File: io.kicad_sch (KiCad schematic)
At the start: 35 parts, among them K2 TIANBO-HJR-4102-L, K3 TIANBO-HJR-4102-L, K4 TIANBO-HJR-4102-L, K5 TIANBO-HJR-4102-L, K6 TIANBO-HJR-4102-L, K7 TIANBO-HJR-4102-L, K8 AQY210S, Q2 BSS138, Q3 BSS138, Q4 BSS138, Q5 BSS138, Q6 BSS138, Q7 BSS138, U10 74HC595, X5 Conn_Rel2, X6 Conn_Rel1

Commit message: Redesign PCB
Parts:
- removed D11: LED1, LED_SMD:LED_PLCC-2, symbol Device:LED_Small
- removed K8: AQY210S, SamacSys_Parts:SOP254P962X275-4N, symbol SamacSys_Parts:AQY210S
- removed R19, R24: 180R, Resistor_SMD:R_0603_1608Metric, symbol Device:R_Small
- added C60: 100n, Capacitor_SMD:C_0603_1608Metric, symbol Device:C_Small
- added J10: JP_REL1_COM_12V, Connector_PinHeader_2.54mm:PinHeader_1x02_P2.54mm_Vertical, symbol Connector:Conn_01x02_Male
- added J12: JP_REL2_COM_12V, Connector_PinHeader_2.54mm:PinHeader_1x02_P2.54mm_Vertical, symbol Connector:Conn_01x02_Male
- added J13: JP_REL3_COM_12V, Connector_PinHeader_2.54mm:PinHeader_1x02_P2.54mm_Vertical, symbol Connector:Conn_01x02_Male
- added J14: Conn_REL1, Connector_PinHeader_2.54mm:PinHeader_1x03_P2.54mm_Vertical, symbol Connector:Conn_01x03_Male
- added J15: Conn_REL2, Connector_PinHeader_2.54mm:PinHeader_1x03_P2.54mm_Vertical, symbol Connector:Conn_01x03_Male
- added J16: Conn_REL3, Connector_PinHeader_2.54mm:PinHeader_1x03_P2.54mm_Vertical, symbol Connector:Conn_01x03_Male
- added J5: JP_REL4_COM_12V, Connector_PinHeader_2.54mm:PinHeader_1x02_P2.54mm_Vertical, symbol Connector:Conn_01x02_Male
- added J8: JP_REL5_COM_12V, Connector_PinHeader_2.54mm:PinHeader_1x02_P2.54mm_Vertical, symbol Connector:Conn_01x02_Male
- added J9: JP_REL6_COM_12V, Connector_PinHeader_2.54mm:PinHeader_1x02_P2.54mm_Vertical, symbol Connector:Conn_01x02_Male
- added JP29: JP_REL_VCC, Jumper:SolderJumper-3_P1.3mm_Open_RoundedPad1.0x1.5mm, symbol Jumper:SolderJumper_3_Open
- added R74, R75, R76, R77, R78, R79: 4k7, Resistor_SMD:R_0603_1608Metric, symbol Device:R_Small
- added U20: HC 151, Package_SO:SOIC-16_3.9x9.9mm_P1.27mm, symbol 74xx_IEEE:74151
- Q5, Q6, Q7: value BSS138 -> IRLML 2502
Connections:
- net DO1_1 is gone; now on net REL6_COM: X5.7 (Pin_7)
- net DO1_2 is gone; now on net REL6_NO: X5.8 (Pin_8)
- net +3V3: now also C60.1, R74.2, R75.2, R76.2, R77.2, R78.2, R79.2, U20.16 (VCC)
- net +5V: now also JP29.1 (A); no longer D10.1 (K), D5.1 (K), D6.1 (K), D7.1 (K), D8.1 (K), D9.1 (K), K2.5, K3.5, K4.5, K5.5, K6.5, K7.5
- net GND: now also C60.2, U20.7 (~{E}), U20.8 (GND); no longer X5.9 (Pin_9)
- net REL1_COM: now also J10.1 (Pin_1)
- net REL1_NC: now also J14.3 (Pin_3); no longer X6.2 (Pin_2)
- net REL1_NO: now also X6.2 (Pin_2); no longer X6.3 (Pin_3)
- net REL2_COM: now also J12.1 (Pin_1)
- net REL2_NC: now also J15.3 (Pin_3); no longer X6.5 (Pin_5)
- net REL2_NO: now also X6.5 (Pin_5); no longer X6.6 (Pin_6)
- net REL3_COM: now also J13.1 (Pin_1)
- net REL3_NC: now also J16.3 (Pin_3); no longer X6.8 (Pin_8)
- net REL3_NO: now also X6.8 (Pin_8); no longer X6.9 (Pin_9)
- net REL4_COM: now also J5.1 (Pin_1)
- net REL5_COM: now also X5.4 (Pin_4), J8.1 (Pin_1); no longer X5.3 (Pin_3)
- net REL5_NO: now also X5.5 (Pin_5); no longer X5.4 (Pin_4)
- net REL6_COM: now also J9.1 (Pin_1); no longer X5.5 (Pin_5)
- net REL6_NO: no longer X5.6 (Pin_6)
- net T_ADDR1: now reaches U10.7 (QH)
- net T_ADDR1: now also U20.10 (S1)
- net DO1 renamed T_ADDR0
- net T_ADDR0: now also U20.11 (S0)
- new net REL1_NC_TACHO: J14.2 (Pin_2), X6.3 (Pin_3)
- new net REL2_NC_TACHO: J15.2 (Pin_2), X6.6 (Pin_6)
- new net REL3_NC_TACHO: J16.2 (Pin_2), X6.9 (Pin_9)
- new net TACHO: U20.5 (Q)
- new net TACHO1: J14.1 (Pin_1), R74.1, U20.4 (I0)
- new net TACHO2: J15.1 (Pin_1), R75.1, U20.3 (I1)
- new net TACHO3: J16.1 (Pin_1), R76.1, U20.2 (I2)
- new net TACHO4: R77.1, U20.1 (I3), X5.3 (Pin_3)
- new net TACHO5: R78.1, U20.15 (I4), X5.6 (Pin_6)
- new net TACHO6: R79.1, U20.14 (I5), X5.9 (Pin_9)
- new net T_ADDR2: U20.9 (S2)
- new net VCC_REL: D10.1 (K), D5.1 (K), D6.1 (K), D7.1 (K), D8.1 (K), D9.1 (K), JP29.2 (C), K2.5, K3.5, K4.5, K5.5, K6.5, K7.5
- new net V_IN: J10.2 (Pin_2), J12.2 (Pin_2), J13.2 (Pin_2), J5.2 (Pin_2), J8.2 (Pin_2), J9.2 (Pin_2), JP29.3 (B)
- no-connect marks 0 -> 3
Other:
- note added: "12V Eingangsspannung auf COM des Relais"
- note added: "J15 - J16: NC des Relais oder Tachosignal auf Stecker"
- note added: "Je nach Relaistyp kann eine Spulenspannung von 5V oder 12V gewählt werden. Wichtig hierfür ist, dass die Bestückung der DC/DC auf Seite beachtet wrid."
- moved on the sheet: C17, C18, R22, R23, U10, X5, X6

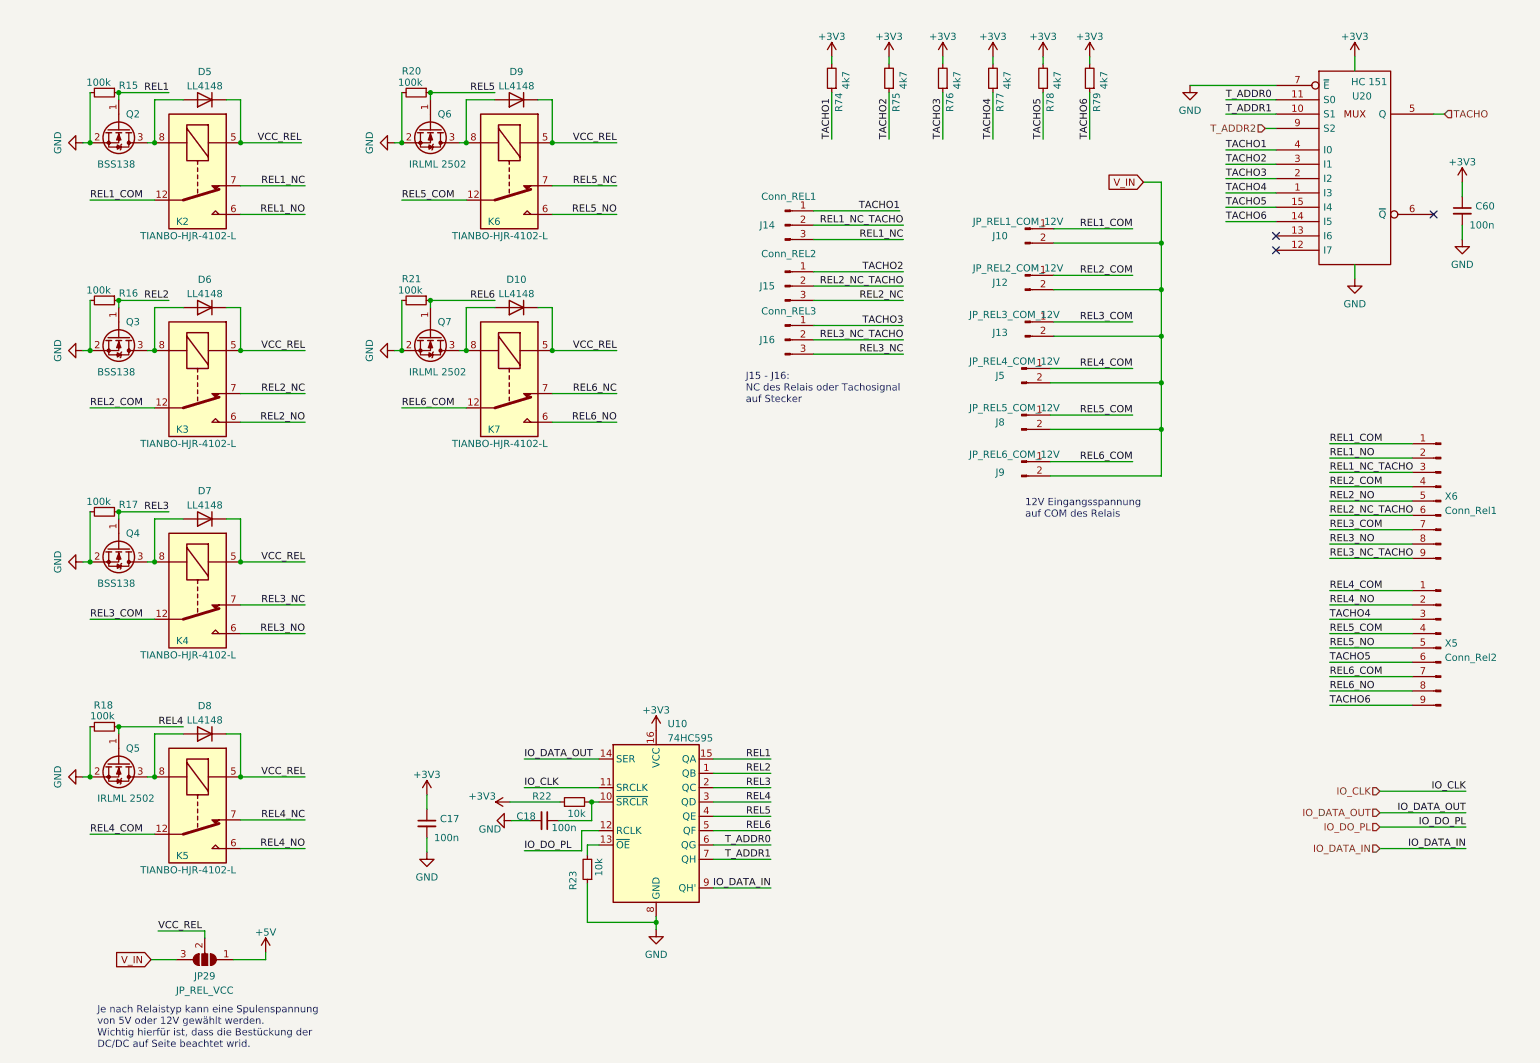
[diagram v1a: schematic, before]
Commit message: Layout optimized
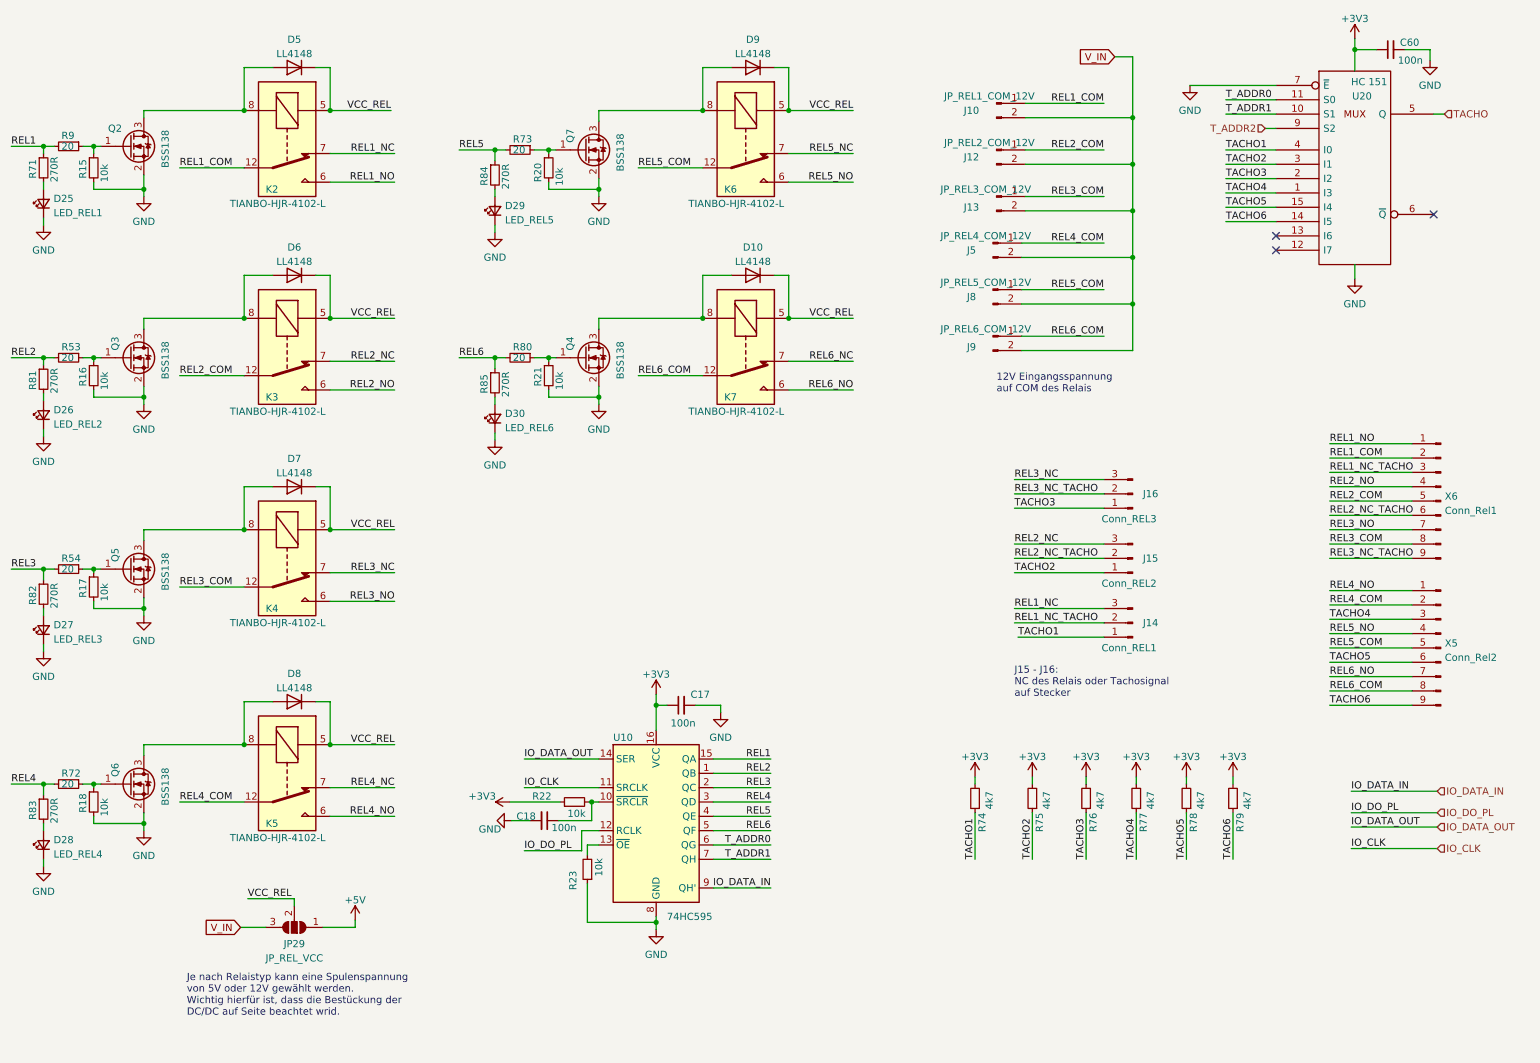
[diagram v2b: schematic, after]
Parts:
- removed Q5: IRLML 2502, Package_TO_SOT_SMD:SOT-23, symbol Transistor_FET:BSS138
- added D25: LED_REL1, LED_SMD:LED_0603_1608Metric, symbol Device:LED_Small
- added D26: LED_REL2, LED_SMD:LED_0603_1608Metric, symbol Device:LED_Small
- added D27: LED_REL3, LED_SMD:LED_0603_1608Metric, symbol Device:LED_Small
- added D28: LED_REL4, LED_SMD:LED_0603_1608Metric, symbol Device:LED_Small
- added D29: LED_REL5, LED_SMD:LED_0603_1608Metric, symbol Device:LED_Small
- added D30: LED_REL6, LED_SMD:LED_0603_1608Metric, symbol Device:LED_Small
- added Q4: BSS138, Package_TO_SOT_SMD:SOT-23, symbol Transistor_FET:BSS138
- added R53, R54, R72, R73, R80, R9: 20, Resistor_SMD:R_0603_1608Metric, symbol Device:R_Small
- added R71, R81, R82, R83, R84, R85: 270R, Resistor_SMD:R_0603_1608Metric, symbol Device:R_Small
- Q6, Q7: value IRLML 2502 -> BSS138
- R15, R16, R17, R18, R20, R21: value 100k -> 10k
- renumbered Q4 to Q5
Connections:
- net GND: now also D25.1 (K), D26.1 (K), D27.1 (K), D28.1 (K), D29.1 (K), D30.1 (K), Q4.2 (S)
- net REL1: now also R71.1, R9.2; no longer Q2.1 (G), R15.1
- net REL1_COM: now also X6.2 (Pin_2); no longer X6.1 (Pin_1)
- net REL1_NO: now also X6.1 (Pin_1); no longer X6.2 (Pin_2)
- net REL2: now also R53.2, R81.1; no longer Q3.1 (G), R16.1
- net REL2_COM: now also X6.5 (Pin_5); no longer X6.4 (Pin_4)
- net REL2_NO: now also X6.4 (Pin_4); no longer X6.5 (Pin_5)
- net REL3: now also R54.2, R82.1; no longer Q5.1 (G), R17.1
- net REL3_COM: now also X6.8 (Pin_8); no longer X6.7 (Pin_7)
- net REL3_NO: now also X6.7 (Pin_7); no longer X6.8 (Pin_8)
- net REL4: now also R72.2, R83.1; no longer R18.1
- net REL4_COM: now also X5.2 (Pin_2); no longer X5.1 (Pin_1)
- net REL4_NO: now also X5.1 (Pin_1); no longer X5.2 (Pin_2)
- net REL5: now also R73.2, R84.1; no longer Q6.1 (G), R20.1
- net REL5_COM: now also X5.5 (Pin_5); no longer X5.4 (Pin_4)
- net REL5_NO: now also X5.4 (Pin_4); no longer X5.5 (Pin_5)
- net REL6: now also R80.2, R85.1; no longer Q7.1 (G), R21.1
- net REL6_COM: now also X5.8 (Pin_8); no longer X5.7 (Pin_7)
- net REL6_NO: now also X5.7 (Pin_7); no longer X5.8 (Pin_8)
- net at D10.2 (A), K7.8: now also Q4.3 (D); no longer Q7.3 (D)
- net at D9.2 (A), K6.8: now also Q7.3 (D); no longer Q6.3 (D)
- net at D8.2 (A), K5.8: now also Q6.3 (D)
- new net: Q7.1 (G), R20.1, R73.1
- new net: D26.2 (A), R81.2
- new net: Q4.1 (G), R21.1, R80.1
- new net: D27.2 (A), R82.2
- new net: Q3.1 (G), R16.1, R53.1
- new net: D29.2 (A), R84.2
- new net: Q6.1 (G), R18.1, R72.1
- new net: D30.2 (A), R85.2
- new net: Q2.1 (G), R15.1, R9.1
- new net: Q5.1 (G), R17.1, R54.1
- new net: D25.2 (A), R71.2
- new net: D28.2 (A), R83.2
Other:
- moved on the sheet: C17, C60, D10, D5, D6, D7, D8, D9, J10, J12, J13, J14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
